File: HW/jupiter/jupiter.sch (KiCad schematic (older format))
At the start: 0 parts

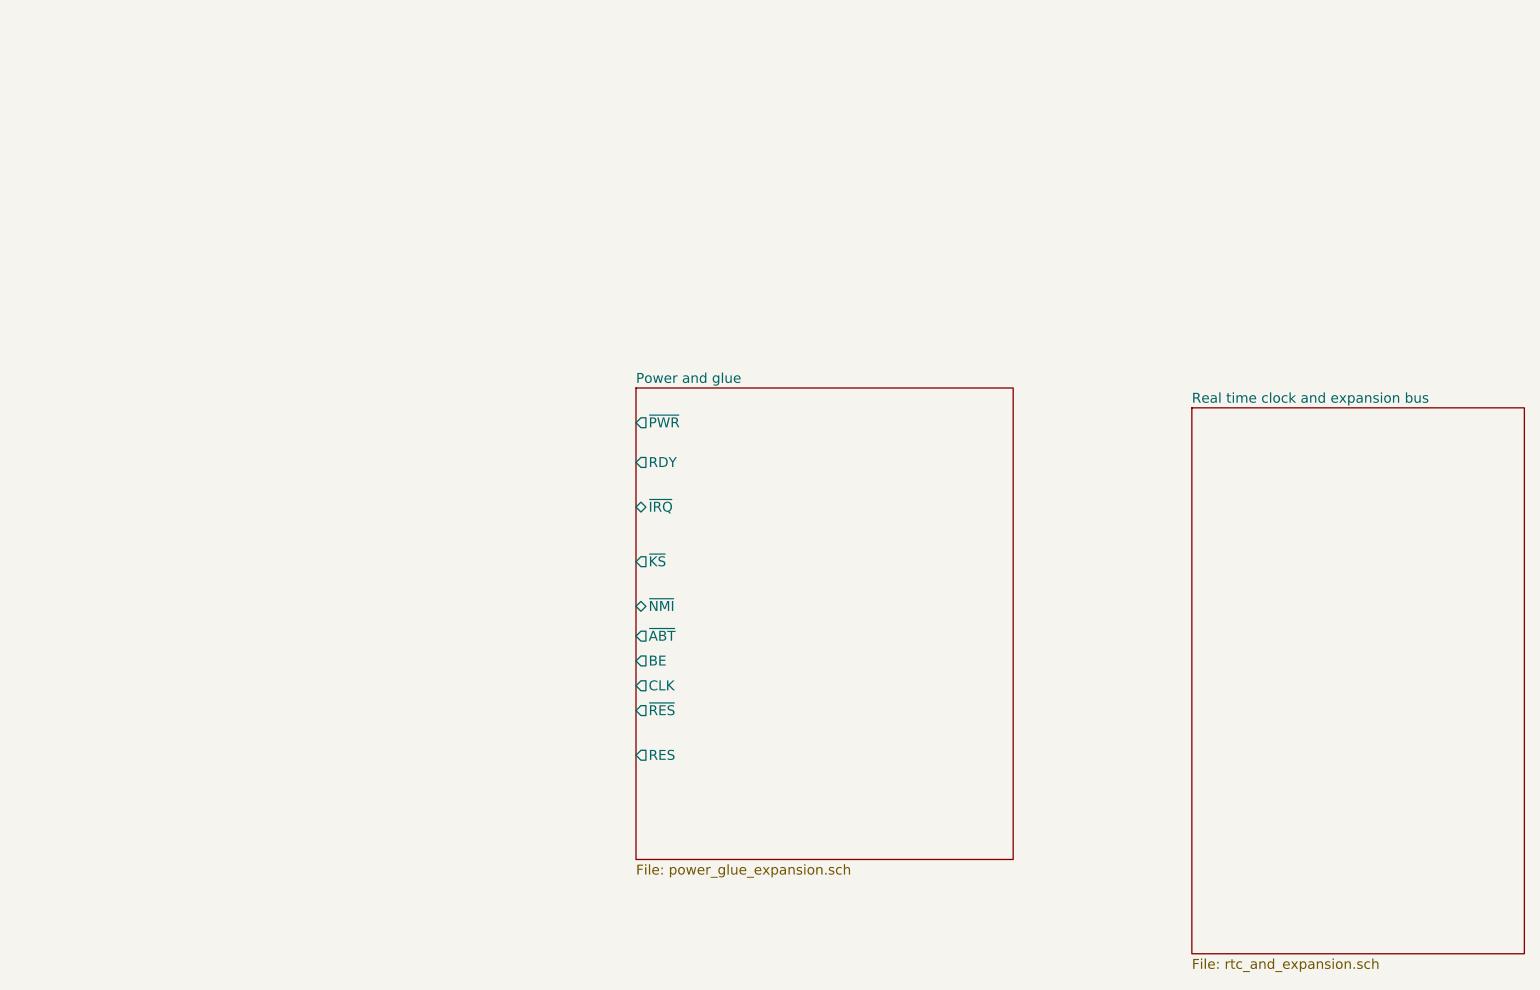
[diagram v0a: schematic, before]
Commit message: Started PCB. CPU, RTC and support section added.
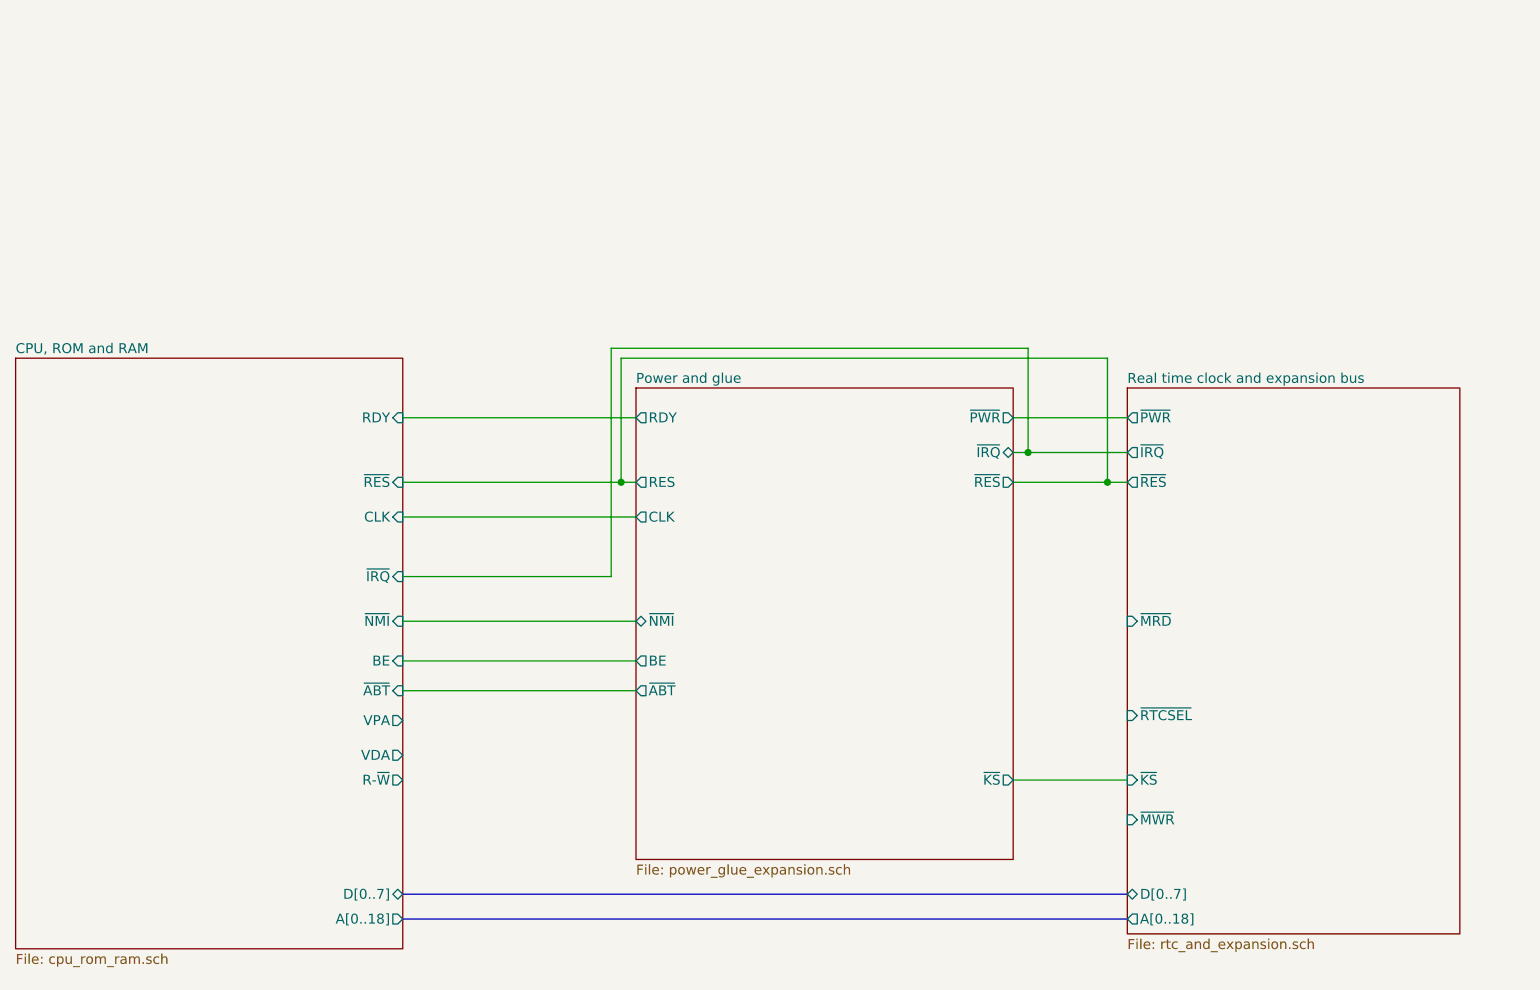
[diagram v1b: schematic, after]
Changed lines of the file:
@@
 $Descr A4 11693 8268
 encoding utf-8
-Sheet 1 3
+Sheet 1 4
 Title ""
 Date ""
@@
 F0 "Power and glue" 50
 F1 "power_glue_expansion.sch" 50
-F2 "~KS" O L 4250 4425 50
-F3 "~IRQ" B L 4250 4150 50
-F4 "~NMI" B L 4250 4650 50
+F2 "~KS" O R 6150 5525 50
+F3 "~IRQ" B R 6150 3875 50
+F4 "~NMI" B L 4250 4725 50
 F5 "BE" O L 4250 4925 50
-F6 "RDY" O L 4250 3925 50
-F7 "~ABT" O L 4250 4800 50
-F8 "~PWR" O L 4250 3725 50
-F9 "~RES" O L 4250 5175 50
-F10 "RES" O L 4250 5400 50
-F11 "CLK" O L 4250 5050 50
+F6 "RDY" O L 4250 3700 50
+F7 "~ABT" O L 4250 5075 50
+F8 "~PWR" O R 6150 3700 50
+F9 "~RES" O R 6150 4025 50
+F10 "RES" O L 4250 4025 50
+F11 "CLK" O L 4250 4200 50
 $EndSheet
 $Sheet
-S 7050 3650 1675 2750
+S 6725 3550 1675 2750
 U 5D100144
 F0 "Real time clock and expansion bus" 50
 F1 "rtc_and_expansion.sch" 50
+F2 "D[0..7]" B L 6725 6100 50
+F3 "A[0..18]" O L 6725 6225 50
+F4 "~IRQ" O L 6725 3875 50
+F5 "~RES" O L 6725 4025 50
+F6 "~PWR" O L 6725 3700 50
+F7 "~KS" I L 6725 5525 50
+F8 "~MWR" I L 6725 5725 50
+F9 "~MRD" I L 6725 4725 50
+F10 "~RTCSEL" I L 6725 5200 50
 $EndSheet
+$Sheet
+S 1125 3400 1950 2975
+U 5D18AF83
+F0 "CPU, ROM and RAM" 50
+F1 "cpu_rom_ram.sch" 50
+F2 "RDY" I R 3075 3700 50
+F3 "~RES" I R 3075 4025 50
+F4 "CLK" I R 3075 4200 50
+F5 "~IRQ" I R 3075 4500 50
+F6 "~NMI" I R 3075 4725 50
+F7 "R-~W" O R 3075 5525 50
+F8 "VPA" O R 3075 5225 50
+F9 "VDA" O R 3075 5400 50
+F10 "BE" I R 3075 4925 50
+F11 "~ABT" I R 3075 5075 50
+F12 "D[0..7]" B R 3075 6100 50
+F13 "A[0..18]" O R 3075 6225 50
+$EndSheet
+Wire Wire Line
+	6725 3700 6150 3700
+Wire Wire Line
+	6150 3875 6225 3875
+Wire Wire Line
+	3075 3700 4250 3700
+Wire Wire Line
+	4250 4025 4175 4025
+Wire Wire Line
+	3075 4200 4250 4200
+Wire Wire Line
+	6150 5525 6725 5525
+Wire Wire Line
+	4175 4025 4175 3400
+Wire Wire Line
+	4175 3400 6625 3400
+Wire Wire Line
+	6625 3400 6625 4025
+Wire Wire Line
+	6625 4025 6725 4025
+Connection ~ 4175 4025
+Wire Wire Line
+	4175 4025 3075 4025
+Wire Wire Line
+	3075 4725 4250 4725
+Wire Wire Line
+	3075 4500 4125 4500
+Wire Wire Line
+	4125 4500 4125 3350
+Wire Wire Line
+	4125 3350 6225 3350
+Wire Wire Line
+	6225 3350 6225 3875
+Connection ~ 6225 3875
+Wire Wire Line
+	6225 3875 6725 3875
+Wire Wire Line
+	6150 4025 6625 4025
+Connection ~ 6625 4025
+Wire Wire Line
+	4250 4925 3075 4925
+Wire Wire Line
+	4250 5075 3075 5075
+Wire Bus Line
+	6725 6225 3075 6225
+Wire Bus Line
+	3075 6100 6725 6100
 $EndSCHEMATC

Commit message: A lot of new data sheets. Some updates to schema and PCB layout.
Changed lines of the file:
@@
 EESchema Schematic File Version 4
 LIBS:jupiter-cache
-EELAYER 29 0
+EELAYER 30 0
 EELAYER END
 $Descr A4 11693 8268
 encoding utf-8
-Sheet 1 4
+Sheet 1 5
 Title ""
 Date ""
@@
 Wire Bus Line
 	3075 6100 6725 6100
+$Sheet
+S 6825 1775 1550 1450
+U 5DAC752C
+F0 "DUART and line drivers" 50
+F1 "duart.sch" 50
+$EndSheet
 $EndSCHEMATC
